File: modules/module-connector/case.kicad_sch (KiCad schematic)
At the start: 5 parts

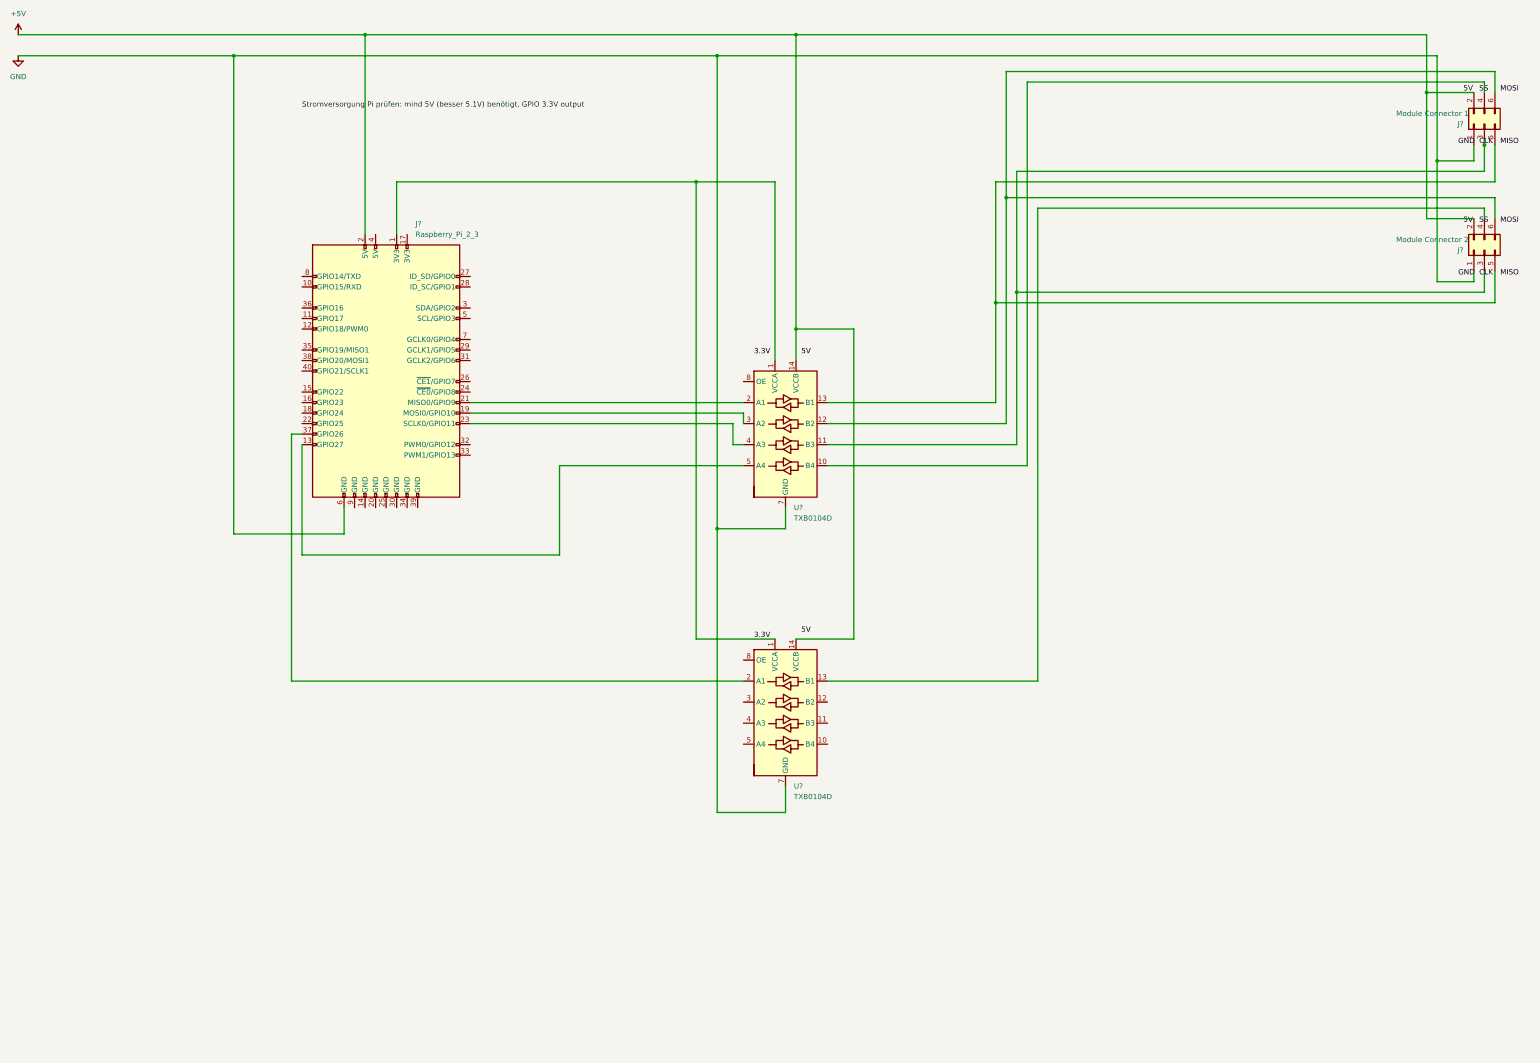
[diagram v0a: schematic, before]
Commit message: cleanup circuit
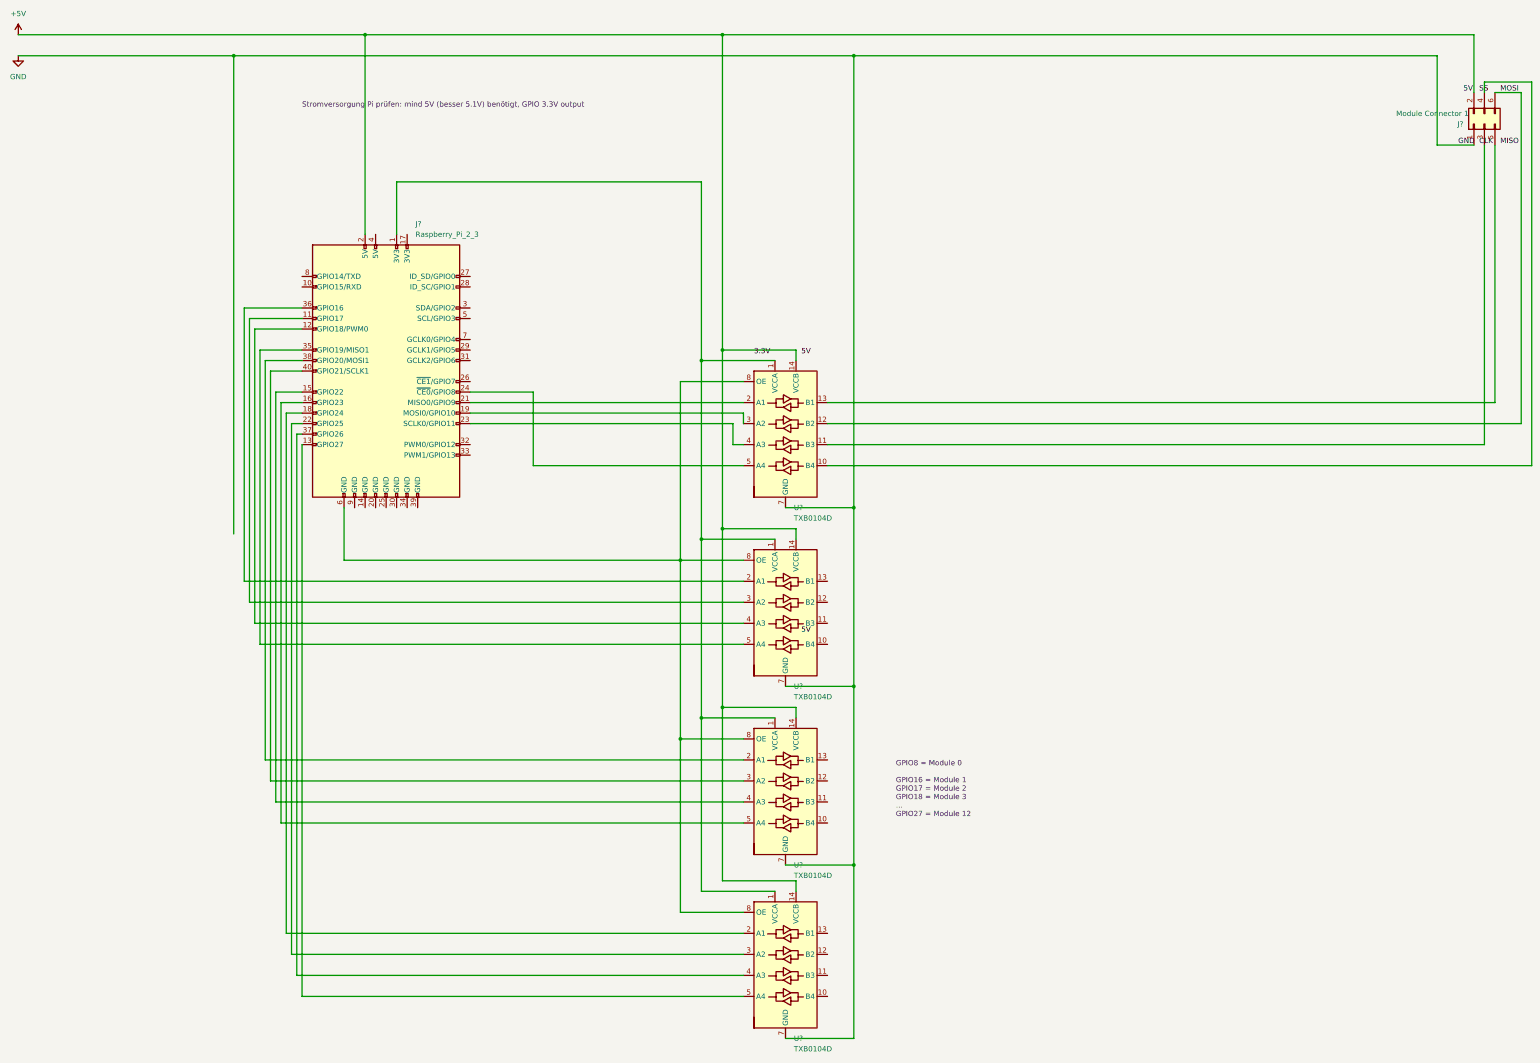
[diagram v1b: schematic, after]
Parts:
- removed J?: Module Connector 2, symbol Connector_Generic:Conn_02x03_Odd_Even
- added U? (x2): TXB0104D, Package_SO:SOIC-14_3.9x8.7mm_P1.27mm, symbol Logic_LevelTranslator:TXB0104D
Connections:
- net +5V: now also U?.14 (VCCB), U?.14 (VCCB)
- net 3.3V: no longer J?.1 (3V3), U?.1 (VCCA), U?.1 (VCCA)
- net GND: now also U?.7 (GND), U?.7 (GND); no longer J?.6 (GND)
- net MOSI: now also J?.6 (Pin_6), U?.12 (B2)
- net at U?.5 (A4): now also J?.24 (~{CE0}/GPIO8); no longer J?.13 (GPIO27)
- net at U?.8 (OE): now also J?.6 (GND), U?.8 (OE), U?.8 (OE), U?.8 (OE)
- net at J?.11 (GPIO17): now also U?.3 (A2)
- net at J?.12 (GPIO18/PWM0): now also U?.4 (A3)
- net at J?.15 (GPIO22): now also U?.4 (A3)
- net at J?.16 (GPIO23): now also U?.5 (A4)
- net at J?.18 (GPIO24): now also U?.2 (A1)
- net at J?.22 (GPIO25): now also U?.3 (A2)
- net at J?.35 (GPIO19/MISO1): now also U?.5 (A4)
- net at J?.36 (GPIO16): now also U?.2 (A1)
- net at J?.37 (GPIO26): now also U?.4 (A3); no longer U?.2 (A1)
- net at J?.38 (GPIO20/MOSI1): now also U?.2 (A1)
- net at J?.40 (GPIO21/SCLK1): now also U?.3 (A2)
- new net: J?.1 (3V3), U?.1 (VCCA), U?.1 (VCCA), U?.1 (VCCA), U?.1 (VCCA)
- new net: J?.13 (GPIO27), U?.5 (A4)
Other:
- note added: "GPIO8 = Module 0 GPIO16 = Module 1 GPIO17 = Module 2 GPIO18 = Module 3 ... GPIO27 = Module 12"
- title: (none) -> Schaltplan Case
- moved on the sheet: U?
